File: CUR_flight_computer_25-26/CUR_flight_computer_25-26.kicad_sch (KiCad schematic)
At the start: 0 parts

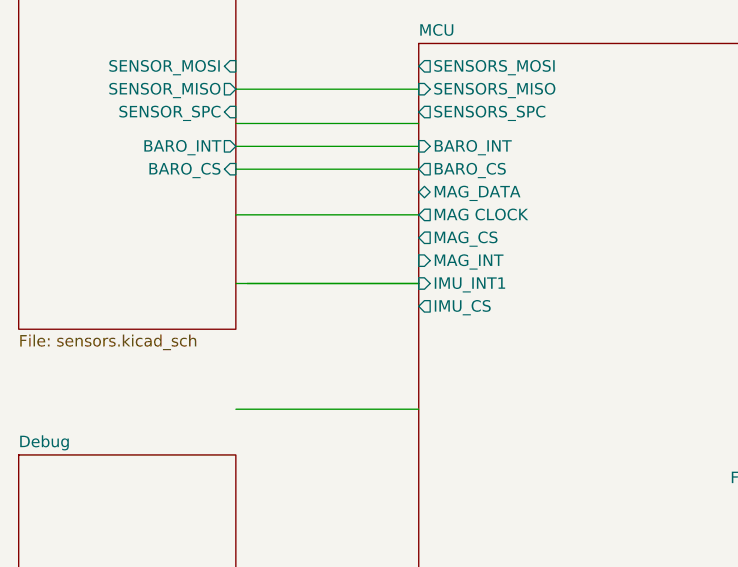
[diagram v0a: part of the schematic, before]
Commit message: added mag
copy pasted magnometer schematic
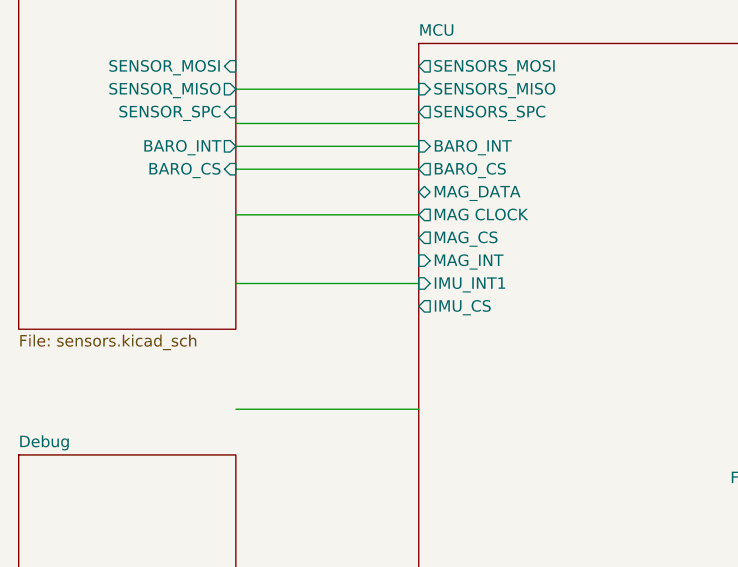
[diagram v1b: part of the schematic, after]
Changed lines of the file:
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@@
+	(wire
+		(pts
+			(xy 93.98 78.74) (xy 114.3 78.74)
+		)
+		(stroke
+			(width 0)
+			(type default)
+		)
+	)
 	(wire
 		(pts
@@
 	(wire
 		(pts
+			(xy 162.56 100.33) (xy 184.15 100.33)
+		)
+		(stroke
+			(width 0)
+			(type default)
+		)
+	)
+	(wire
+		(pts
+			(xy 162.56 97.79) (xy 184.15 97.79)
+		)
+		(stroke
+			(width 0)
+			(type default)
+		)
+	)
+	(wire
+		(pts
 			(xy 148.59 130.81) (xy 148.59 139.7)
 		)
@@
 	(wire
 		(pts
+			(xy 162.56 90.17) (xy 184.15 90.17)
+		)
+		(stroke
+			(width 0)
+			(type default)
+		)
+	)
+	(wire
+		(pts
 			(xy 153.67 130.81) (xy 153.67 139.7)
 		)
@@
 	(wire
 		(pts
-			(xy 93.98 78.74) (xy 114.3 78.74)
-		)
-		(stroke
-			(width 0)
-			(type default)
-		)
-	)
-	(wire
-		(pts
-			(xy 162.56 100.33) (xy 184.15 100.33)
-		)
-		(stroke
-			(width 0)
-			(type default)
-		)
-	)
-	(wire
-		(pts
-			(xy 162.56 97.79) (xy 184.15 97.79)
-		)
-		(stroke
-			(width 0)
-			(type default)
-		)
-	)
-	(wire
-		(pts
-			(xy 162.56 90.17) (xy 184.15 90.17)
-		)
-		(stroke
-			(width 0)
-			(type default)
-		)
-	)
-	(wire
-		(pts
 			(xy 93.98 66.04) (xy 114.3 66.04)
 		)
@@
 	(wire
 		(pts
+			(xy 93.98 63.5) (xy 114.3 63.5)
+		)
+		(stroke
+			(width 0)
+			(type default)
+		)
+	)
+	(wire
+		(pts
 			(xy 161.29 130.81) (xy 161.29 139.7)
 		)
@@
 	(wire
 		(pts
-			(xy 93.98 63.5) (xy 114.3 63.5)
-		)
-		(stroke
-			(width 0)
-			(type default)
-		)
-	)
-	(wire
-		(pts
 			(xy 93.98 57.15) (xy 114.3 57.15)
 		)
@@
 	(wire
 		(pts
+			(xy 151.13 130.81) (xy 151.13 139.7)
+		)
+		(stroke
+			(width 0)
+			(type default)
+		)
+	)
+	(wire
+		(pts
 			(xy 93.98 92.71) (xy 114.3 92.71)
 		)
@@
 	(wire
 		(pts
-			(xy 151.13 130.81) (xy 151.13 139.7)
-		)
-		(stroke
-			(width 0)
-			(type default)
-		)
-	)
-	(wire
-		(pts
 			(xy 93.98 60.96) (xy 114.3 60.96)
 		)
@@
 		(pts
 			(xy 162.56 92.71) (xy 184.15 92.71)
-		)
-		(stroke
-			(width 0)
-			(type default)
-		)
-	)
-	(wire
-		(pts
-			(xy 114.3 78.74) (xy 95.25 78.74)
 		)
 		(stroke
@@
 		(pin "BUZZER" output
 			(at 114.3 123.19 180)
+			(effects
+				(font
+					(size 1.27 1.27)
+				)
+				(justify left)
+			)
 		)
 		(pin "FLASH_CS" output

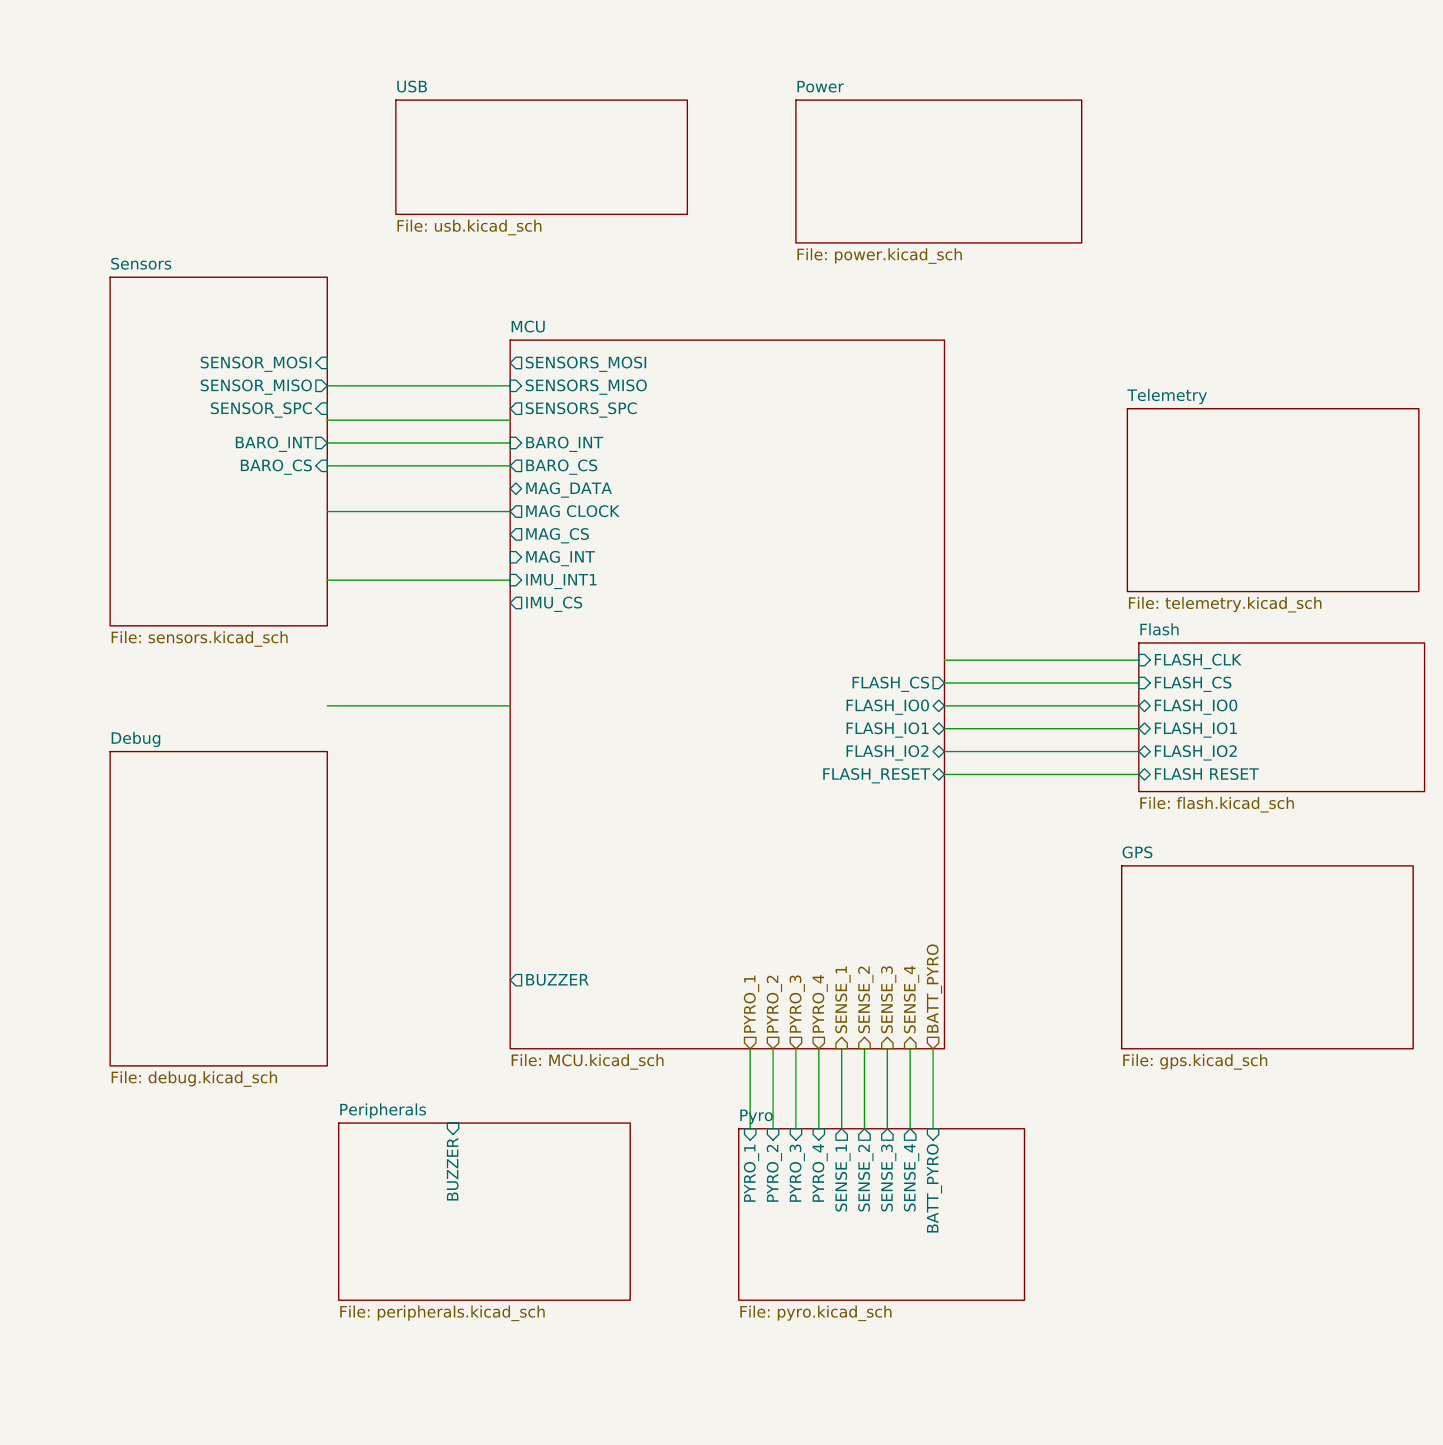
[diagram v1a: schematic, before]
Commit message: updated pins
updated all sensor pins
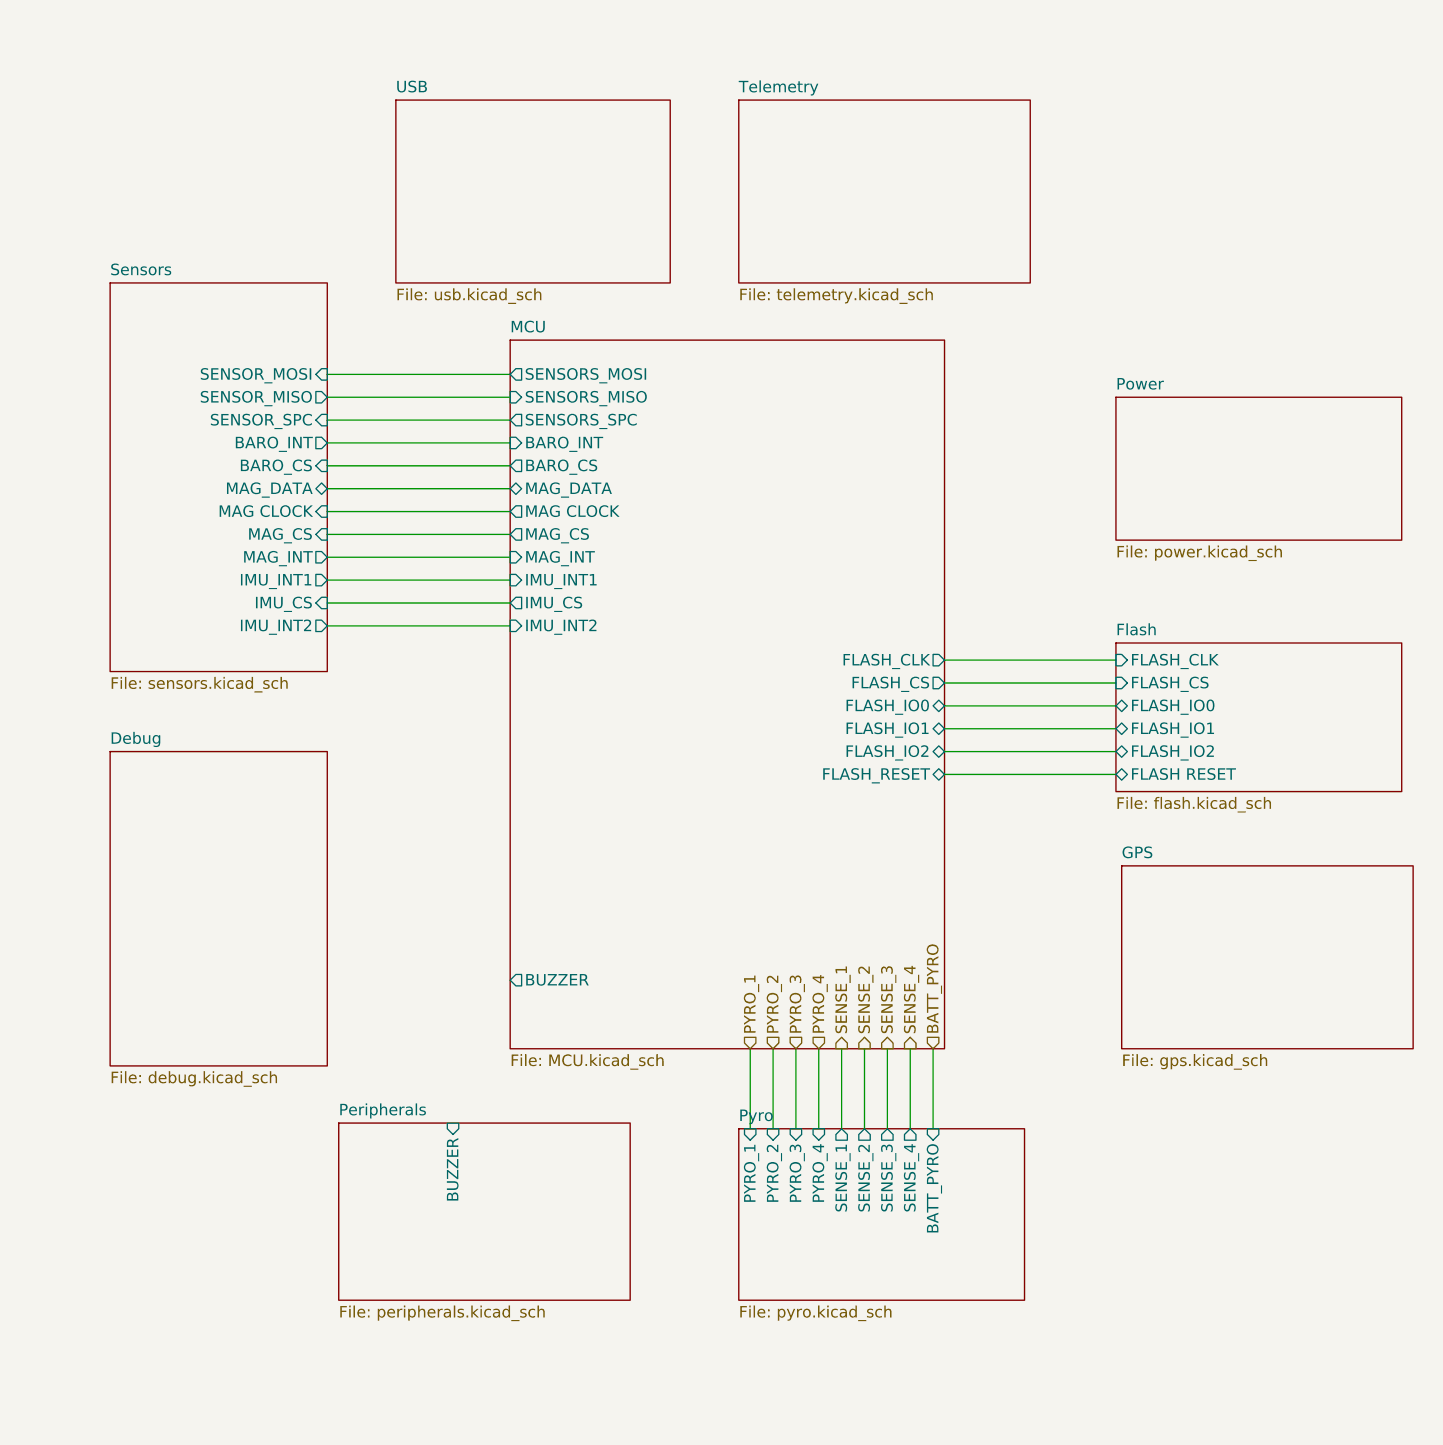
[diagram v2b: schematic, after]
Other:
- sheet MCU ports: added FLASH_CLK, IMU_INT2; removed none
- sheet Sensors ports: added IMU_CS, IMU_INT1, IMU_INT2, MAG CLOCK, MAG_CS, MAG_DATA, MAG_INT; removed none
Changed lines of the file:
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@@
 	(wire
 		(pts
-			(xy 162.56 100.33) (xy 184.15 100.33)
-		)
-		(stroke
-			(width 0)
-			(type default)
-		)
-	)
-	(wire
-		(pts
-			(xy 162.56 97.79) (xy 184.15 97.79)
+			(xy 162.56 100.33) (xy 181.61 100.33)
+		)
+		(stroke
+			(width 0)
+			(type default)
+		)
+	)
+	(wire
+		(pts
+			(xy 93.98 73.66) (xy 114.3 73.66)
+		)
+		(stroke
+			(width 0)
+			(type default)
+		)
+	)
+	(wire
+		(pts
+			(xy 93.98 68.58) (xy 114.3 68.58)
+		)
+		(stroke
+			(width 0)
+			(type default)
+		)
+	)
+	(wire
+		(pts
+			(xy 162.56 97.79) (xy 181.61 97.79)
+		)
+		(stroke
+			(width 0)
+			(type default)
+		)
+	)
+	(wire
+		(pts
+			(xy 93.98 83.82) (xy 114.3 83.82)
 		)
 		(stroke
@@
 	(wire
 		(pts
-			(xy 162.56 90.17) (xy 184.15 90.17)
+			(xy 162.56 90.17) (xy 181.61 90.17)
 		)
 		(stroke
@@
 	(wire
 		(pts
+			(xy 93.98 55.88) (xy 114.3 55.88)
+		)
+		(stroke
+			(width 0)
+			(type default)
+		)
+	)
+	(wire
+		(pts
 			(xy 143.51 130.81) (xy 143.51 139.7)
 		)
@@
 	(wire
 		(pts
-			(xy 162.56 95.25) (xy 184.15 95.25)
+			(xy 162.56 95.25) (xy 181.61 95.25)
+		)
+		(stroke
+			(width 0)
+			(type default)
+		)
+	)
+	(wire
+		(pts
+			(xy 93.98 81.28) (xy 114.3 81.28)
 		)
 		(stroke
@@
 	(wire
 		(pts
-			(xy 93.98 57.15) (xy 114.3 57.15)
+			(xy 93.98 58.42) (xy 114.3 58.42)
 		)
 		(stroke
@@
 	(wire
 		(pts
-			(xy 93.98 92.71) (xy 114.3 92.71)
-		)
-		(stroke
-			(width 0)
-			(type default)
-		)
-	)
-	(wire
-		(pts
 			(xy 93.98 71.12) (xy 114.3 71.12)
 		)
@@
 	(wire
 		(pts
-			(xy 162.56 87.63) (xy 184.15 87.63)
-		)
-		(stroke
-			(width 0)
-			(type default)
-		)
-	)
-	(wire
-		(pts
-			(xy 162.56 92.71) (xy 184.15 92.71)
+			(xy 93.98 76.2) (xy 114.3 76.2)
+		)
+		(stroke
+			(width 0)
+			(type default)
+		)
+	)
+	(wire
+		(pts
+			(xy 162.56 87.63) (xy 181.61 87.63)
+		)
+		(stroke
+			(width 0)
+			(type default)
+		)
+	)
+	(wire
+		(pts
+			(xy 162.56 92.71) (xy 181.61 92.71)
 		)
 		(stroke
@@
 	)
 	(sheet
-		(at 182.88 59.69)
+		(at 139.7 25.4)
 		(size 32.385 20.32)
 		(exclude_from_sim no)
@@
 		)
 		(property "Sheetname" "Telemetry"
-			(at 182.88 58.9784 0)
+			(at 139.7 24.6884 0)
 			(effects
 				(font
@@
 		)
 		(property "Sheetfile" "telemetry.kicad_sch"
-			(at 182.88 80.5946 0)
+			(at 139.7 46.3046 0)
 			(effects
 				(font
@@
 	)
 	(sheet
-		(at 146.05 25.4)
+		(at 181.61 58.42)
 		(size 31.75 15.875)
 		(exclude_from_sim no)
@@
 		)
 		(property "Sheetname" "Power"
-			(at 146.05 24.6884 0)
+			(at 181.61 57.7084 0)
 			(effects
 				(font
@@
 		)
 		(property "Sheetfile" "power.kicad_sch"
-			(at 146.05 41.8596 0)
+			(at 181.61 74.8796 0)
 			(effects
 				(font
@@
 		)
 		(pin "SENSORS_MISO" input
-			(at 114.3 57.15 180)
+			(at 114.3 58.42 180)
 			(effects
 				(font
@@
 		)
 		(pin "SENSORS_MOSI" output
-			(at 114.3 54.61 180)
+			(at 114.3 55.88 180)
 			(effects
 				(font
@@
 		)
 		(pin "SENSORS_SPC" output
-			(at 114.3 59.69 180)
+			(at 114.3 60.96 180)
 			(effects
 				(font
@@
 		(pin "FLASH_RESET" bidirectional
 			(at 162.56 100.33 0)
+			(effects
+				(font
+					(size 1.27 1.27)
+				)
+				(justify right)
+			)
+		)
+		(pin "IMU_INT2" input
+			(at 114.3 83.82 180)
+			(effects
+				(font
+					(size 1.27 1.27)
+				)
+				(justify left)
+			)
+		)
+		(pin "FLASH_CLK" output
+			(at 162.56 87.63 0)
 			(effects
 				(font
@@
 	)
 	(sheet
-		(at 184.15 85.725)
+		(at 181.61 85.725)
 		(size 31.75 16.51)
 		(exclude_from_sim no)
@@
 		)
 		(property "Sheetname" "Flash"
-			(at 184.15 85.0134 0)
+			(at 181.61 85.0134 0)
 			(effects
 				(font
@@
 		)
 		(property "Sheetfile" "flash.kicad_sch"
-			(at 184.15 102.8196 0)
+			(at 181.61 102.8196 0)
 			(effects
 				(font
@@
 		)
 		(pin "FLASH RESET" bidirectional
-			(at 184.15 100.33 180)
+			(at 181.61 100.33 180)
 			(effects
 				(font
@@
 		)
 		(pin "FLASH_CLK" input
-			(at 184.15 87.63 180)
+			(at 181.61 87.63 180)
 			(effects
 				(font
@@
 		)
 		(pin "FLASH_CS" input
-			(at 184.15 90.17 180)
+			(at 181.61 90.17 180)
 			(effects
 				(font
@@
 		)
 		(pin "FLASH_IO0" bidirectional
-			(at 184.15 92.71 180)
+			(at 181.61 92.71 180)
 			(effects
 				(font
@@
 		)
 		(pin "FLASH_IO2" bidirectional
-			(at 184.15 97.79 180)
+			(at 181.61 97.79 180)
 			(effects
 				(font
@@
 		)
 		(pin "FLASH_IO1" bidirectional
-			(at 184.15 95.25 180)
+			(at 181.61 95.25 180)
 			(effects
 				(font
@@
 	)
 	(sheet
-		(at 69.85 45.085)
-		(size 24.13 38.735)
+		(at 69.85 45.72)
+		(size 24.13 43.18)
 		(exclude_from_sim no)
 		(in_bom yes)
@@
 		)
 		(property "Sheetname" "Sensors"
-			(at 69.85 44.3734 0)
+			(at 69.85 45.0084 0)
 			(effects
 				(font
@@
 		)
 		(property "Sheetfile" "sensors.kicad_sch"
-			(at 69.85 84.4046 0)
+			(at 69.85 89.4846 0)
 			(effects
 				(font
@@
 		)
 		(pin "SENSOR_SPC" input
-			(at 93.98 59.69 0)
+			(at 93.98 60.96 0)
 			(effects
 				(font
@@
 		)
 		(pin "SENSOR_MISO" output
-			(at 93.98 57.15 0)
+			(at 93.98 58.42 0)
 			(effects
 				(font
@@
 		)
 		(pin "SENSOR_MOSI" input
-			(at 93.98 54.61 0)
+			(at 93.98 55.88 0)
+			(effects
+				(font
+					(size 1.27 1.27)
+				)
+				(justify right)
+			)
+		)
+		(pin "MAG_INT" output
+			(at 93.98 76.2 0)
+			(effects
+				(font
+					(size 1.27 1.27)
+				)
+				(justify right)
+			)
+		)
+		(pin "MAG_DATA" bidirectional
+			(at 93.98 68.58 0)
+			(effects
+				(font
+					(size 1.27 1.27)
+				)
+				(justify right)
+			)
+		)
+		(pin "MAG CLOCK" input
+			(at 93.98 71.12 0)
+			(effects
+				(font
+					(size 1.27 1.27)
+				)
+				(justify right)
+			)
+		)
+		(pin "IMU_CS" input
+			(at 93.98 81.28 0)
+			(effects
+				(font
+					(size 1.27 1.27)
+				)
+				(justify right)
+			)
+		)
+		(pin "IMU_INT1" output
+			(at 93.98 78.74 0)
+			(effects
+				(font
+					(size 1.27 1.27)
+				)
+				(justify right)
+			)
+		)
+		(pin "MAG_CS" input
+			(at 93.98 73.66 0)
+			(effects
+				(font
+					(size 1.27 1.27)
+				)
+				(justify right)
+			)
+		)
+		(pin "IMU_INT2" output
+			(at 93.98 83.82 0)
 			(effects
 				(font
@@
 	(sheet
 		(at 101.6 25.4)
-		(size 32.385 12.7)
+		(size 30.48 20.32)
 		(exclude_from_sim no)
 		(in_bom yes)
@@
 		)
 		(property "Sheetfile" "usb.kicad_sch"
-			(at 101.6 38.6846 0)
-			(effects
-				(font
+			(at 101.6 46.3046 0)
+			(effects
+				(font
